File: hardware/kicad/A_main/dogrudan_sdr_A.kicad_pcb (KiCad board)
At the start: 6 copper layers, 235 x 225 mm, 264 parts, among them J1 XT60, J10 JTAG 2x3, J20 SMA A1, J21 SMA B1, J22 SMA A2, J23 SMA B2, J30 SMA TX1, J31 SMA TX2, J32 SMA TX3, J33 SMA TX4, J40 HR911130A, J41 HR911130A, J60 GPS modul, J61 SMA 10MHz ref, J62 DAC modul, J63 C kartina, J64 UART 3.3V, J65 C kartina #2, J66 D kartina, Q1 DMP3098L, SW1 PROG, T1 ADT1-1WT+, T10 ADT1-1WT+, T11 ADT1-1WT+, T12 ADT1-1WT+, T13 ADT1-1WT+, T2 ADT1-1WT+, T3 ADT1-1WT+, T4 ADT1-1WT+, U1 TPS62130, U10 LFE5U-25F-7BG256I, U11 W25Q128JVSIQ, U15 ADCLK846BCPZ, U16 SN65LVDS2DBVR, U17 SN65LVDS2DBVR, U2 TPS62130, U20 AD9251BCPZ-80, U21 AD9251BCPZ-80, U3 TPS7A2033, U30 AD9767ASTZ, U31 AD9767ASTZ, U4 ADP150, U40 RTL8211FI-CG, U41 RTL8211FI-CG, U5 ADP150, U50 W9825G6KH-6I, U6 ADP150, U62 TLV3501AIDBVR, U7 ADP150, U8 ADP150, U9 ADP150, Y10 ABLNO-V-80.000MHZ, Y610 25MHz, Y626 25MHz

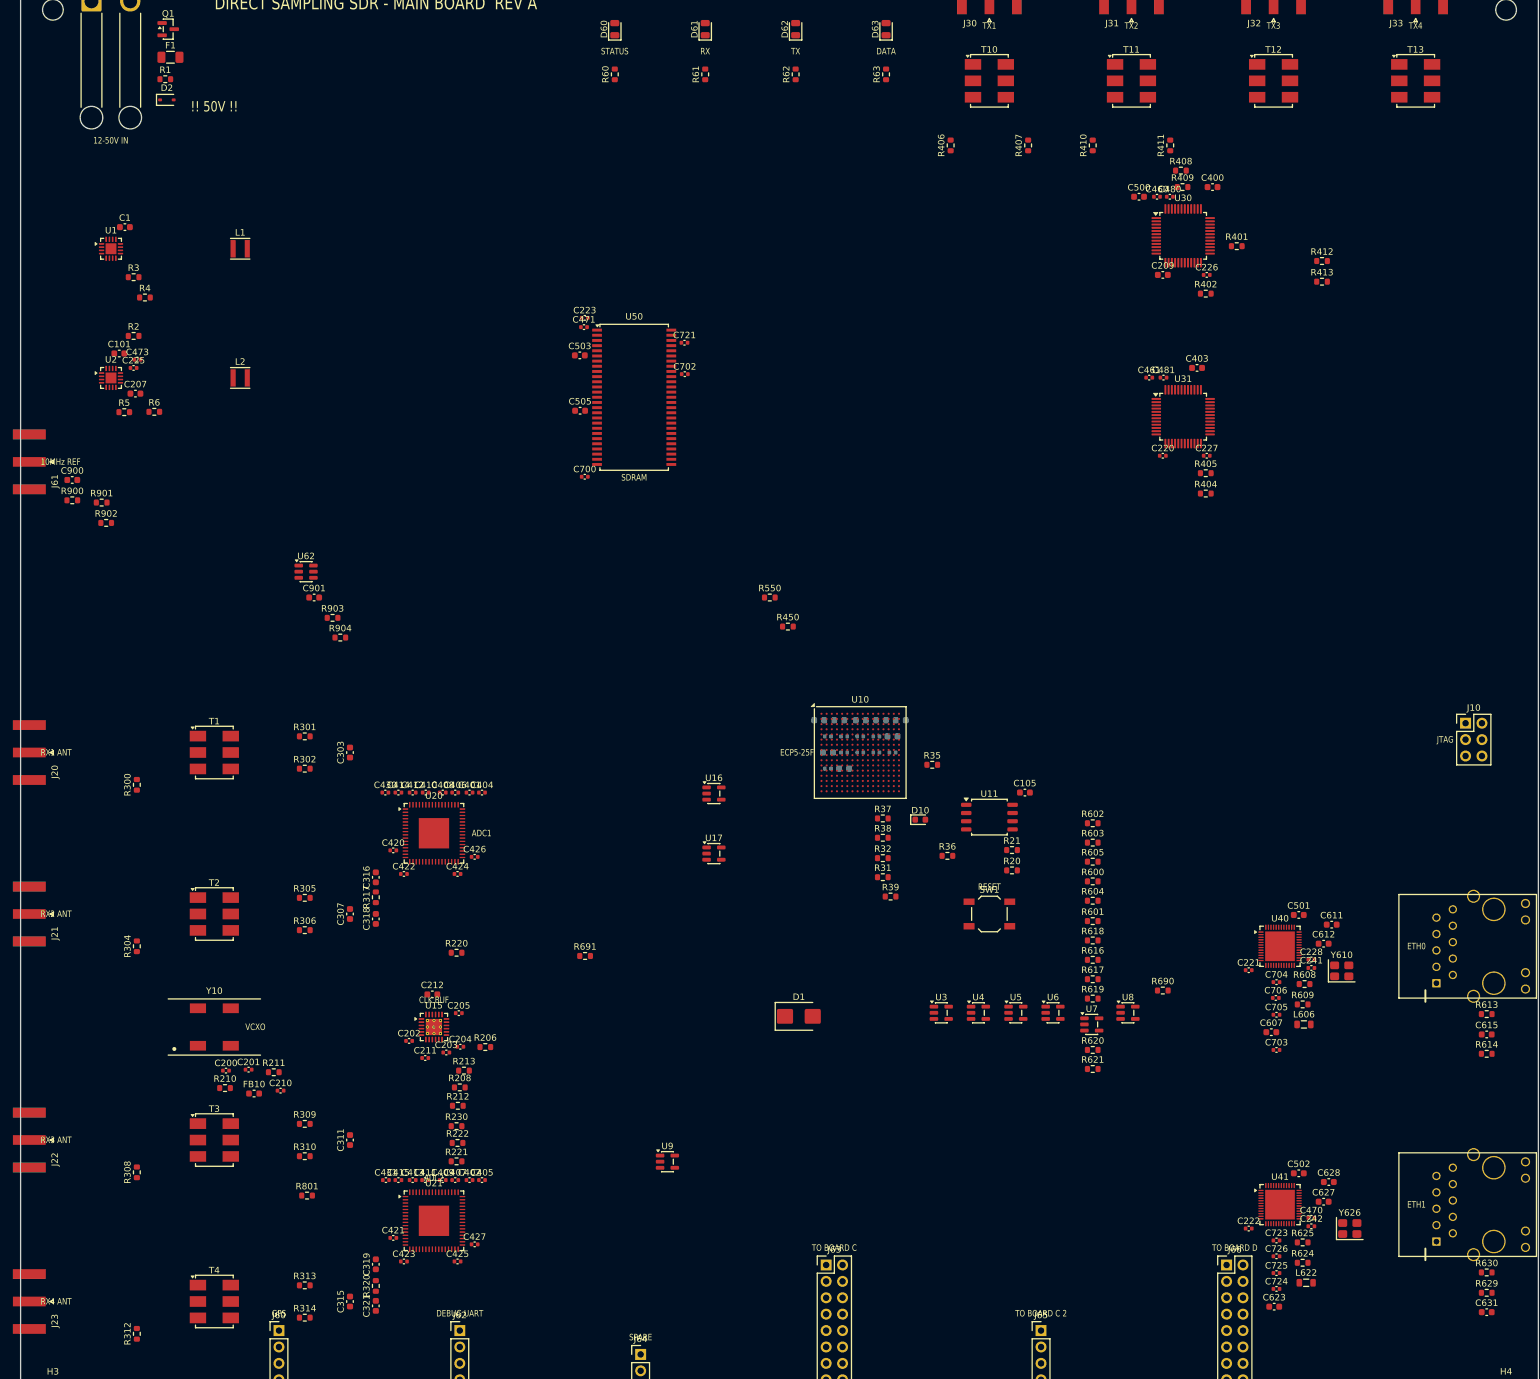
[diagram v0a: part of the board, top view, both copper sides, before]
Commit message: Update the hardware tools and add the gateware
This commit makes the public tree equal to the development tree. The
public tree was behind. It did not have the verification tools, the
build chain, or the FPGA source.

The hardware/kicad directory now has the full tool chain. This
includes yap.sh, which runs the steps in the correct order, and the
tools that check the boards.

The gateware directory is new. It has the Verilog source for the
Lattice ECP5, the test benches, and the synthesis script. The
gateware does the four-channel receive chain, the transmit chain, the
packet interface, and the control interface.

The internal Turkish documents stay in the development tree. The
documentation in this repository is English. The comments in the
source code stay in Turkish.
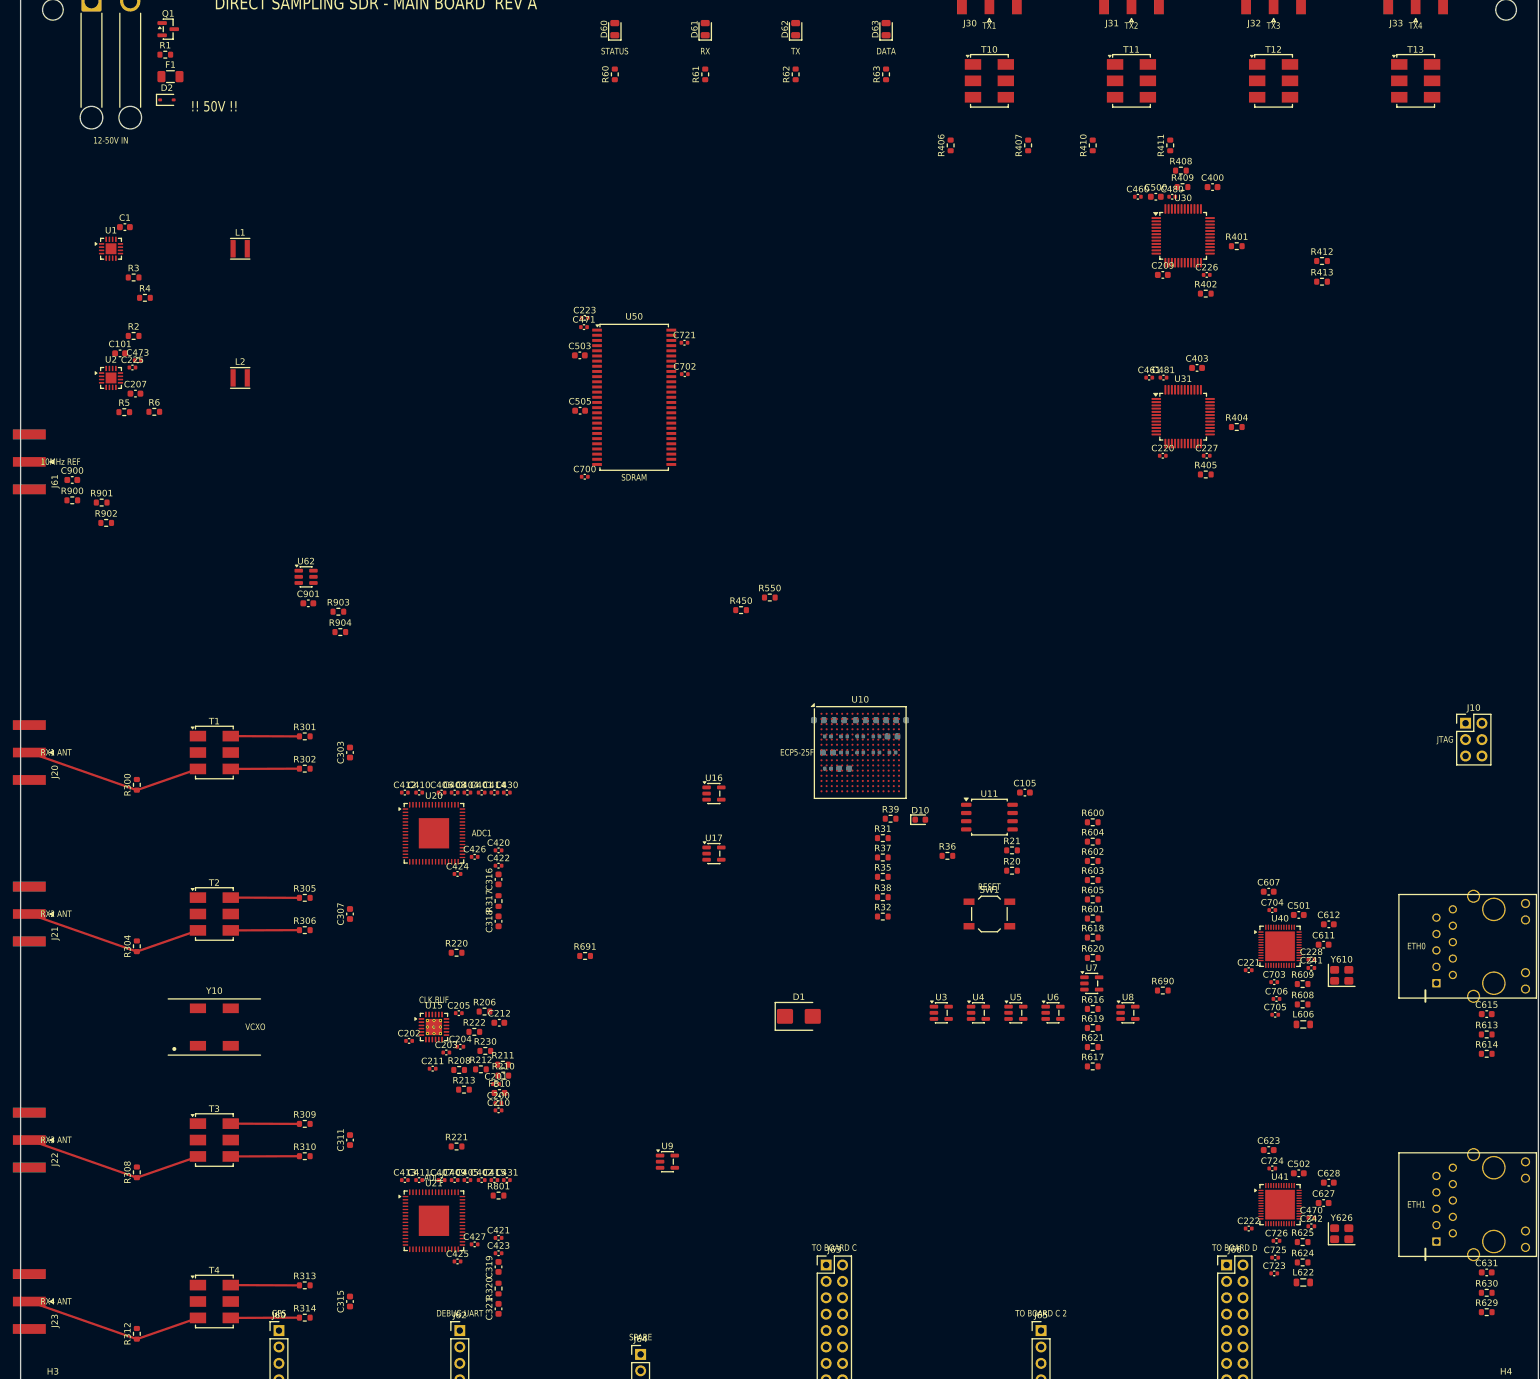
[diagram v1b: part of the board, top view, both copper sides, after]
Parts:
- moved R210 43.1 mm to (74.7, 170.0)
- moved C200 42.5 mm to (74.0, 174.3)
- moved C201 38.4 mm to (73.6, 171.3)
- moved FB10 38.0 mm to (74.1, 172.7)
- moved R211 35.5 mm to (74.7, 168.3)
- moved C210 33.9 mm to (74.0, 175.4)
- moved R801 29.6 mm to (74.0, 188.6)
- moved C623 24.3 mm to (193.2, 181.6)
- moved C607 21.8 mm to (193.2, 141.6)
- moved R317 19.0 mm to (74.0, 143.0)
- moved C321 19.0 mm to (74.0, 206.1)
- moved C319 19.0 mm to (74.0, 199.6)
- moved R320 19.0 mm to (74.0, 203.0)
- moved C318 19.0 mm to (74.0, 146.1)
- moved C316 19.0 mm to (74.0, 139.6)
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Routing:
- net RF_B2: track 0.00 -> 27.7 mm
- net RF_B1: track 0.00 -> 27.7 mm
- net RF_A2: track 0.00 -> 27.7 mm
- net RF_A1: track 0.00 -> 27.7 mm
- net SEC_B2_P: track 0.00 -> 10.6 mm
- net SEC_B2_N: track 0.00 -> 10.6 mm
- net SEC_B1_P: track 0.00 -> 10.6 mm
- net SEC_B1_N: track 0.00 -> 10.6 mm
- net SEC_A2_P: track 0.00 -> 10.6 mm
- net SEC_A2_N: track 0.00 -> 10.6 mm
- net SEC_A1_P: track 0.00 -> 10.6 mm
- net SEC_A1_N: track 0.00 -> 10.6 mm
